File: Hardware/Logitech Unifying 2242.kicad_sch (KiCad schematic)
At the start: 11 parts, among them J1 Bus_M.2_Socket_B, J2 USB, U1 TPS613222ADBV

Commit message: Finish layout and routing
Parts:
- added C1.2, C1.3: 10uF, Capacitor_SMD:C_0805_2012Metric_Pad1.18x1.45mm_HandSolder, symbol Device:C
- C1.1: renamed from C1; value 22uF -> 10uF; footprint (none) -> Capacitor_SMD:C_0805_2012Metric_Pad1.18x1.45mm_HandSolder
- C2: value C -> 150pF; footprint (none) -> Capacitor_SMD:C_0603_1608Metric_Pad1.08x0.95mm_HandSolder
- C3.1: renamed from C3; footprint (none) -> Capacitor_SMD:C_0603_1608Metric_Pad1.08x0.95mm_HandSolder
- C3.2: renamed from C4; footprint (none) -> Capacitor_SMD:C_0805_2012Metric_Pad1.18x1.45mm_HandSolder
- C3.3: renamed from C5; footprint (none) -> Capacitor_SMD:C_0805_2012Metric_Pad1.18x1.45mm_HandSolder
- D1: footprint (none) -> Diode_SMD:D_SMA
- J2: footprint (none) -> Connector_USB:USB_A_TE_292303-7_Horizontal
- L1: footprint (none) -> Inductor_SMD:L_1008_2520Metric_Pad1.43x2.20mm_HandSolder
- R1: value R_US -> 5; footprint (none) -> Resistor_SMD:R_0805_2012Metric_Pad1.20x1.40mm_HandSolder
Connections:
- net +5V: now also C1.2.1, C1.3.1
- net GND: now also C1.2.2, C1.3.2
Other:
- moved on the sheet: C1.1, C2, C3.1, C3.2, C3.3, D1, J1, J2, L1, R1, U1

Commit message: Update M.2 footprints
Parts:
- J1: footprint Connector_OTHER:M.2-2242-B+M-KEY -> Connector_OTHER:M.2-2242-B+M-KEY_USB-ONLY

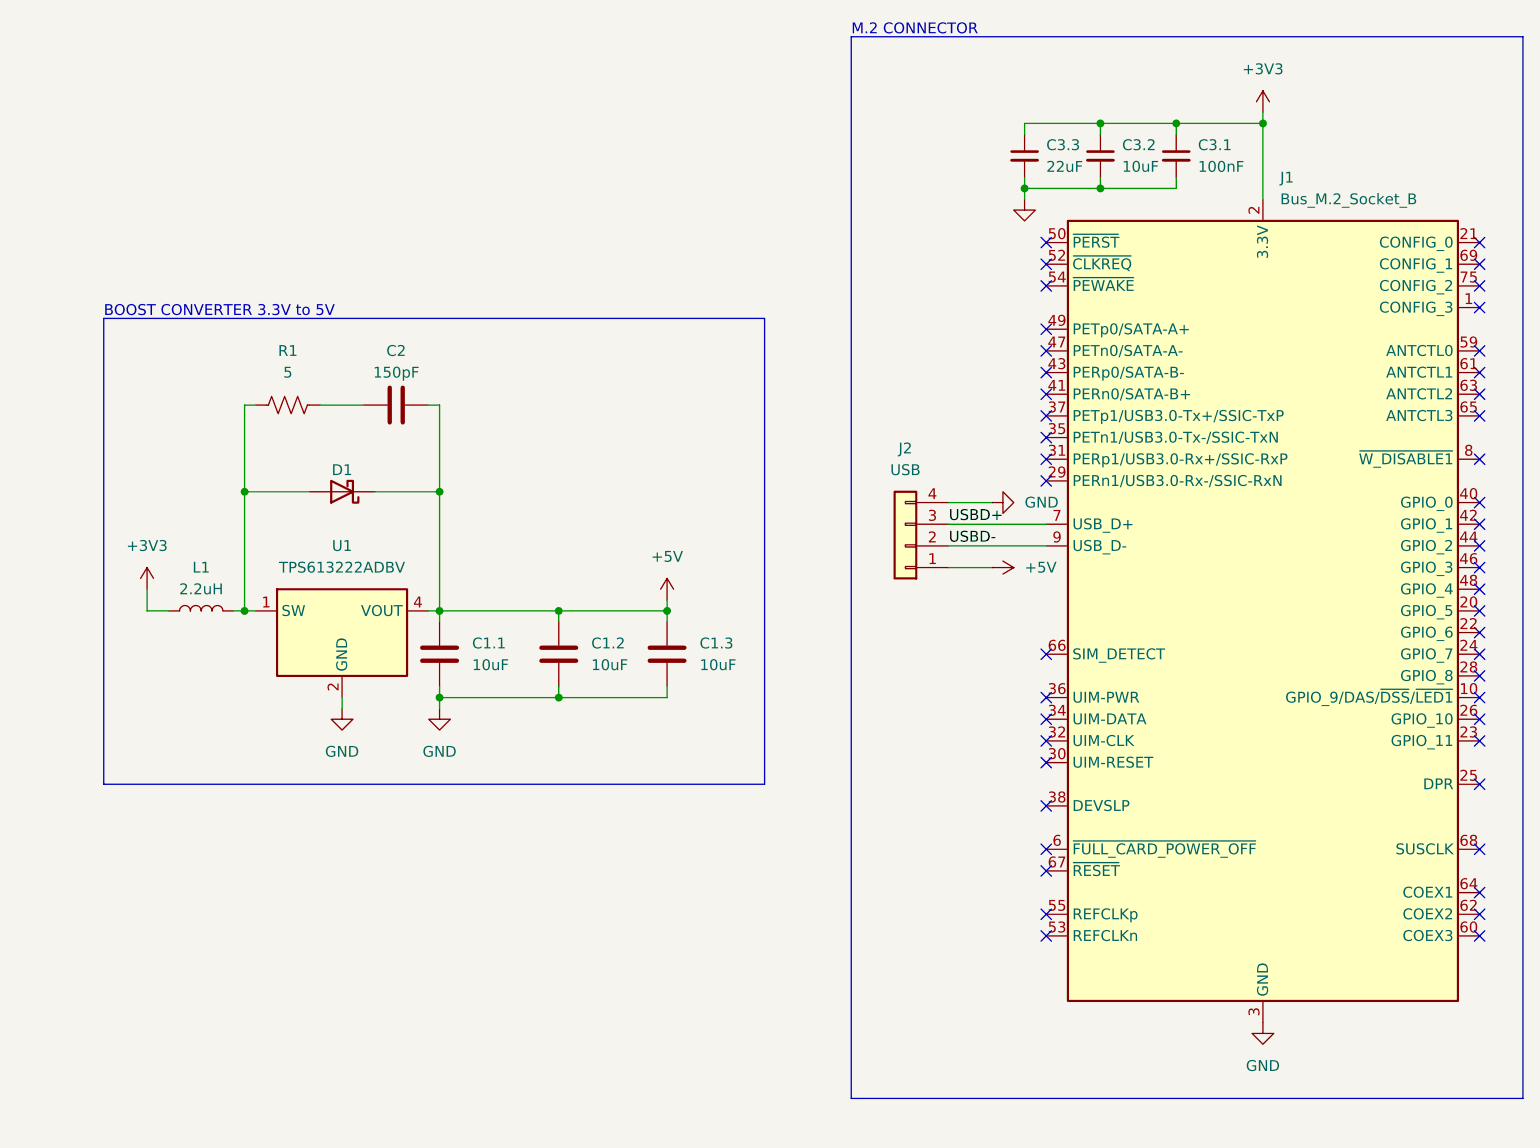
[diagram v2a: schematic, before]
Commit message: Reroute after added fuse and new footprints
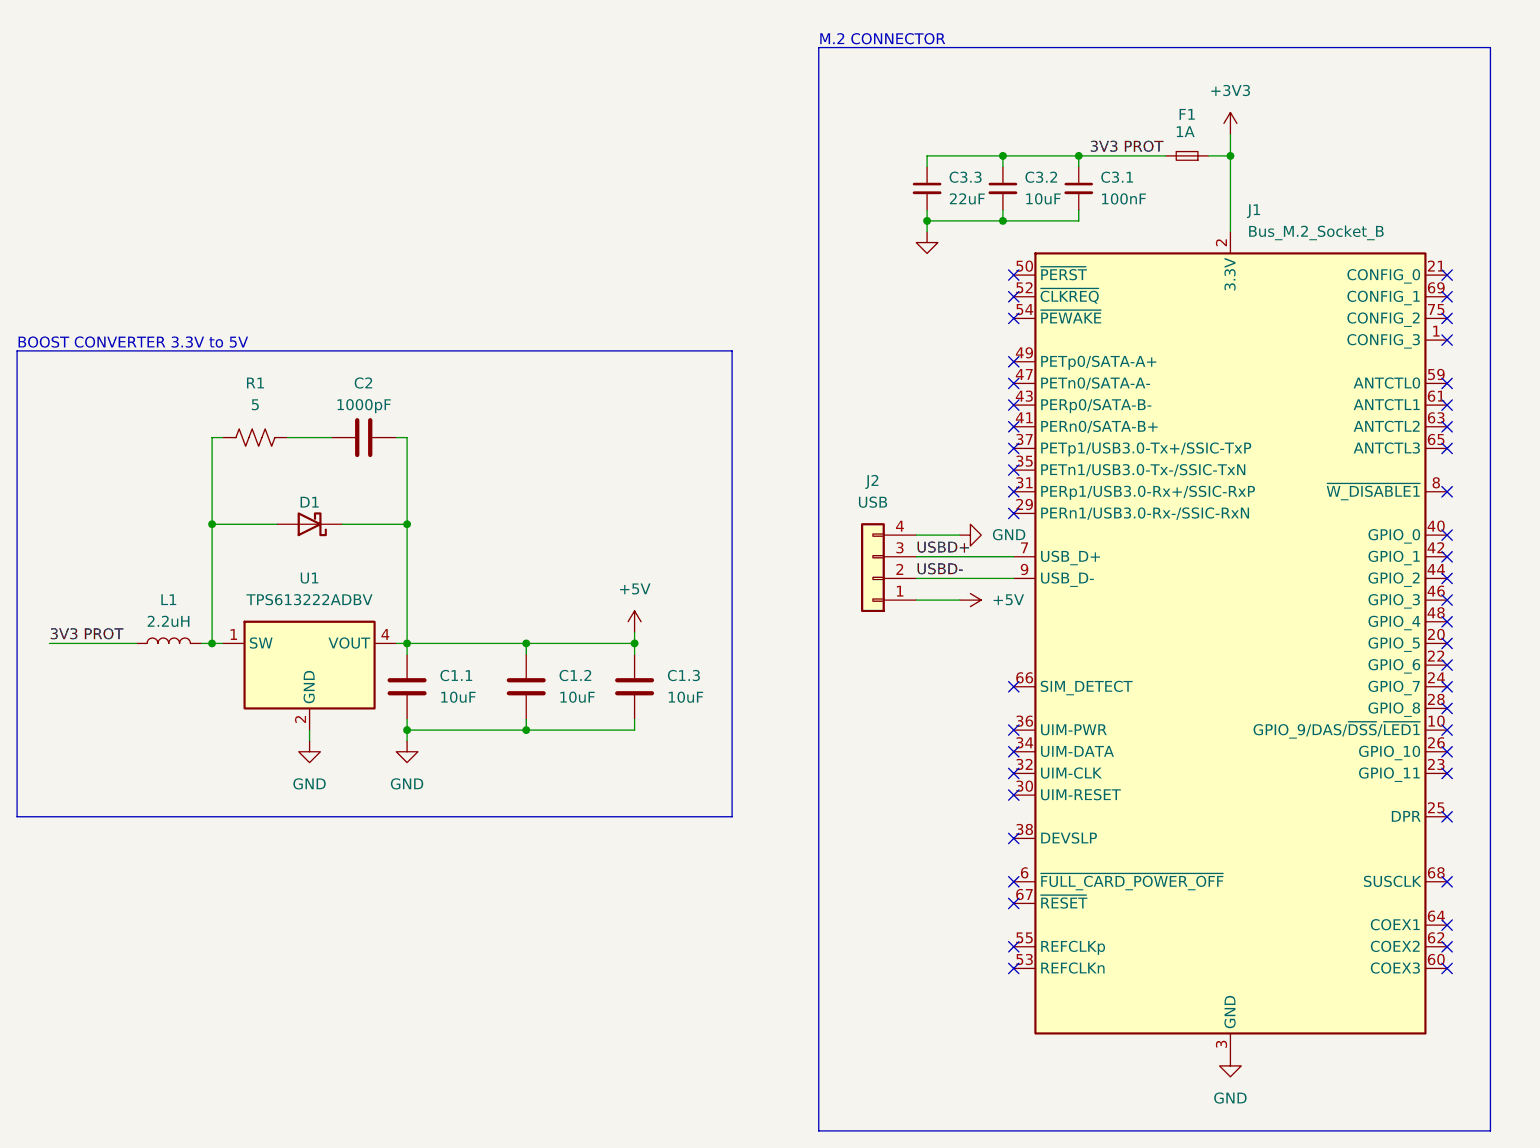
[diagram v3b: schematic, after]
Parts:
- added F1: 1A, Fuse:Fuse_0603_1608Metric_Pad1.05x0.95mm_HandSolder, symbol Device:Fuse_Small
- C1.1, C1.2, C1.3, C3.2, C3.3: footprint Capacitor_SMD:C_0805_2012Metric_Pad1.18x1.45mm_HandSolder -> Capacitor_SMD:C_0402_1005Metric_Pad0.74x0.62mm_HandSolder
- C2: value 150pF -> 1000pF; footprint Capacitor_SMD:C_0603_1608Metric_Pad1.08x0.95mm_HandSolder -> Capacitor_SMD:C_0402_1005Metric_Pad0.74x0.62mm_HandSolder
- C3.1: footprint Capacitor_SMD:C_0603_1608Metric_Pad1.08x0.95mm_HandSolder -> Capacitor_SMD:C_0402_1005Metric_Pad0.74x0.62mm_HandSolder
- D1: footprint Diode_SMD:D_SMA -> Diode_SMD:D_SOD-323
- R1: footprint Resistor_SMD:R_0805_2012Metric_Pad1.20x1.40mm_HandSolder -> Resistor_SMD:R_0402_1005Metric_Pad0.72x0.64mm_HandSolder
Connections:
- net +3V3: now also F1.1; no longer C3.1.1, C3.2.1, C3.3.1, L1.1
- new net 3V3 PROT: C3.1.1, C3.2.1, C3.3.1, F1.2, L1.1
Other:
- moved on the sheet: C1.1, C1.2, C1.3, C2, C3.1, C3.2, C3.3, D1, J1, J2, L1, R1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

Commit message: Add test points (#1) and other finishing touches
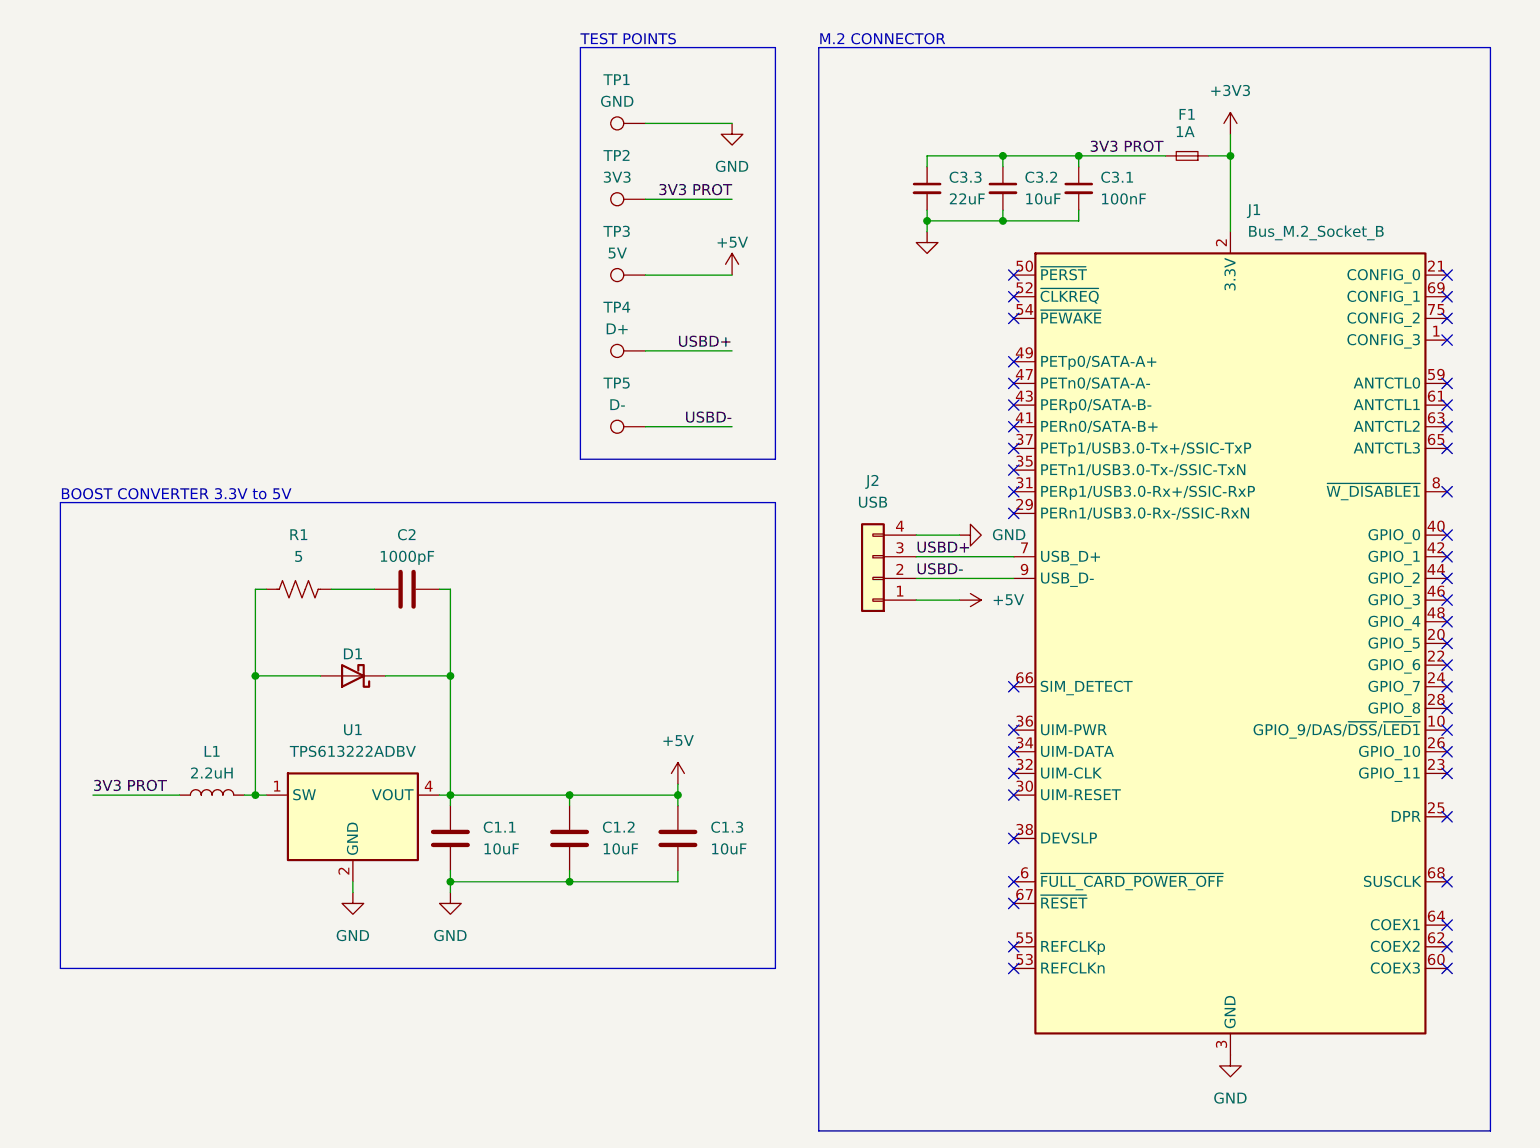
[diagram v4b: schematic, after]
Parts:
- added TP1: GND, TestPoint:TestPoint_Pad_D1.0mm, symbol Connector:TestPoint
- added TP2: 3V3, TestPoint:TestPoint_Pad_D1.0mm, symbol Connector:TestPoint
- added TP3: 5V, TestPoint:TestPoint_Pad_D1.0mm, symbol Connector:TestPoint
- added TP4: D+, TestPoint:TestPoint_Pad_D1.0mm, symbol Connector:TestPoint
- added TP5: D-, TestPoint:TestPoint_Pad_D1.0mm, symbol Connector:TestPoint
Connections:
- net +5V: now also TP3.1
- net 3V3 PROT: now also TP2.1
- net GND: now also TP1.1
- net USBD+: now also TP4.1
- net USBD-: now also TP5.1
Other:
- note added: "TEST POINTS"
- moved on the sheet: C1.1, C1.2, C1.3, C2, D1, L1, R1, U1

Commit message: Add missing net names
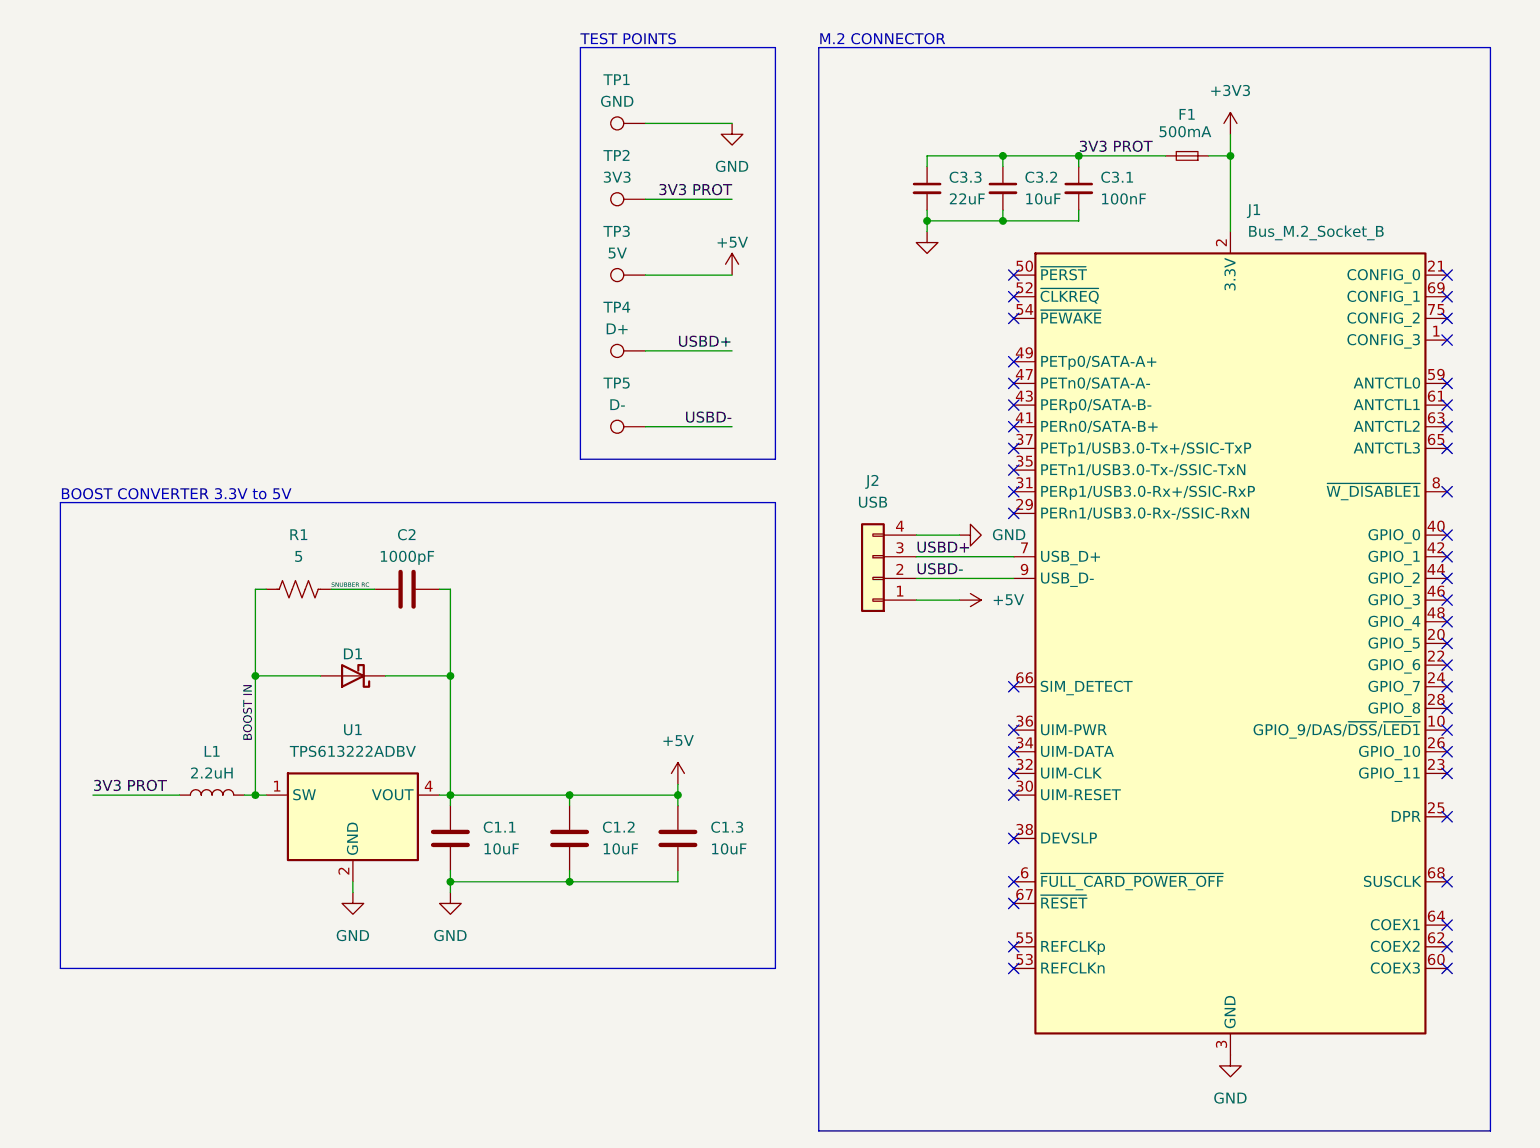
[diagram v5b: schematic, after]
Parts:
- F1: value 1A -> 500mA
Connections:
- net BOOST IN: now reaches D1.2 (A), L1.2, R1.1, U1.1 (SW)
- net SNUBBER RC: now reaches C2.1, R1.2
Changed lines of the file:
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@@
     (effects (font (size 1.27 1.27)) (justify left bottom))
+  )
+  (label "BOOST IN" (at 72.39 110.49 90) (fields_autoplaced)
+    (effects (font (size 1 1)) (justify left bottom))
   )
   (label "USBD-" (at 128.27 73.66 180) (fields_autoplaced)
@@
     (effects (font (size 1.27 1.27)) (justify left bottom))
   )
-  (label "3V3 PROT" (at 170.18 41.91 0) (fields_autoplaced)
+  (label "3V3 PROT" (at 168.91 41.91 0) (fields_autoplaced)
     (effects (font (size 1.27 1.27)) (justify left bottom))
   )
@@
   (label "3V3 PROT" (at 128.27 46.99 180) (fields_autoplaced)
     (effects (font (size 1.27 1.27)) (justify right bottom))
+  )
+  (label "SNUBBER RC" (at 81.28 92.71 0) (fields_autoplaced)
+    (effects (font (size 0.5 0.5)) (justify left bottom))
   )
   (label "3V3 PROT" (at 53.34 116.84 0) (fields_autoplaced)
@@
       (effects (font (size 1.27 1.27)))
     )
-    (property "Value" "1A" (at 181.356 39.116 0)
-      (effects (font (size 1.27 1.27)))
-    )
+    (property "Value" "500mA" (at 181.356 39.116 0)
+      (effects (font (size 1.27 1.27)))
+    )
